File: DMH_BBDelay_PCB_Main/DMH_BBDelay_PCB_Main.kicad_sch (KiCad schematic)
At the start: 0 parts

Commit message: Started designing schematic
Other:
- added sheet Attenuverters (Attenuverters.kicad_sch)
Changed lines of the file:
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@@
 		)
 		(instances
-			(project "DMH-Kosmo-10cm-PCB"
+			(project "DMH_BBDelay_PCB_Main"
 				(path "/58f4306d-5387-4983-bb08-41a2313fd315"
 					(page "4")
@@
 		)
 		(instances
-			(project "DMH-Kosmo-10cm-PCB"
+			(project "DMH_BBDelay_PCB_Main"
 				(path "/58f4306d-5387-4983-bb08-41a2313fd315"
 					(page "3")
@@
 		)
 		(instances
-			(project "DMH-Kosmo-10cm-PCB"
+			(project "DMH_BBDelay_PCB_Main"
 				(path "/58f4306d-5387-4983-bb08-41a2313fd315"
 					(page "2")
 				)
 			)
+		)
+	)
+	(sheet
+		(at 63.5 152.4)
+		(size 25.4 25.4)
+		(exclude_from_sim no)
+		(in_bom yes)
+		(on_board yes)
+		(dnp no)
+		(fields_autoplaced yes)
+		(stroke
+			(width 0.1524)
+			(type solid)
+		)
+		(fill
+			(color 0 0 0 0)
+		)
+		(property "Sheetname" "Attenuverters"
+			(at 63.5 151.6884 0)
+			(show_name no)
+			(do_not_autoplace no)
+			(effects
+				(font
+					(size 1.27 1.27)
+					(thickness 0.254)
+					(bold yes)
+					(italic yes)
+				)
+				(justify left bottom)
+			)
+		)
+		(property "Sheetfile" "Attenuverters.kicad_sch"
+			(at 63.5 178.3846 0)
+			(hide yes)
+			(show_name no)
+			(do_not_autoplace no)
+			(effects
+				(font
+					(size 1.27 1.27)
+				)
+				(justify left top)
+			)
+		)
+		(instances
+			(project "DMH_BBDelay_PCB_Main"
+				(path "/58f4306d-5387-4983-bb08-41a2313fd315"
+					(page "6")
+				)
+			)

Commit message: Schematic in progress
Next is implementation of Channel B, CV Linking and Ping-Pong mode
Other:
- title: (none) -> 3205 Delay
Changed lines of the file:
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@@
 	(paper "A4")
 	(title_block
+		(title "3205 Delay")
 		(rev "1")
 		(company "DMH Instruments")

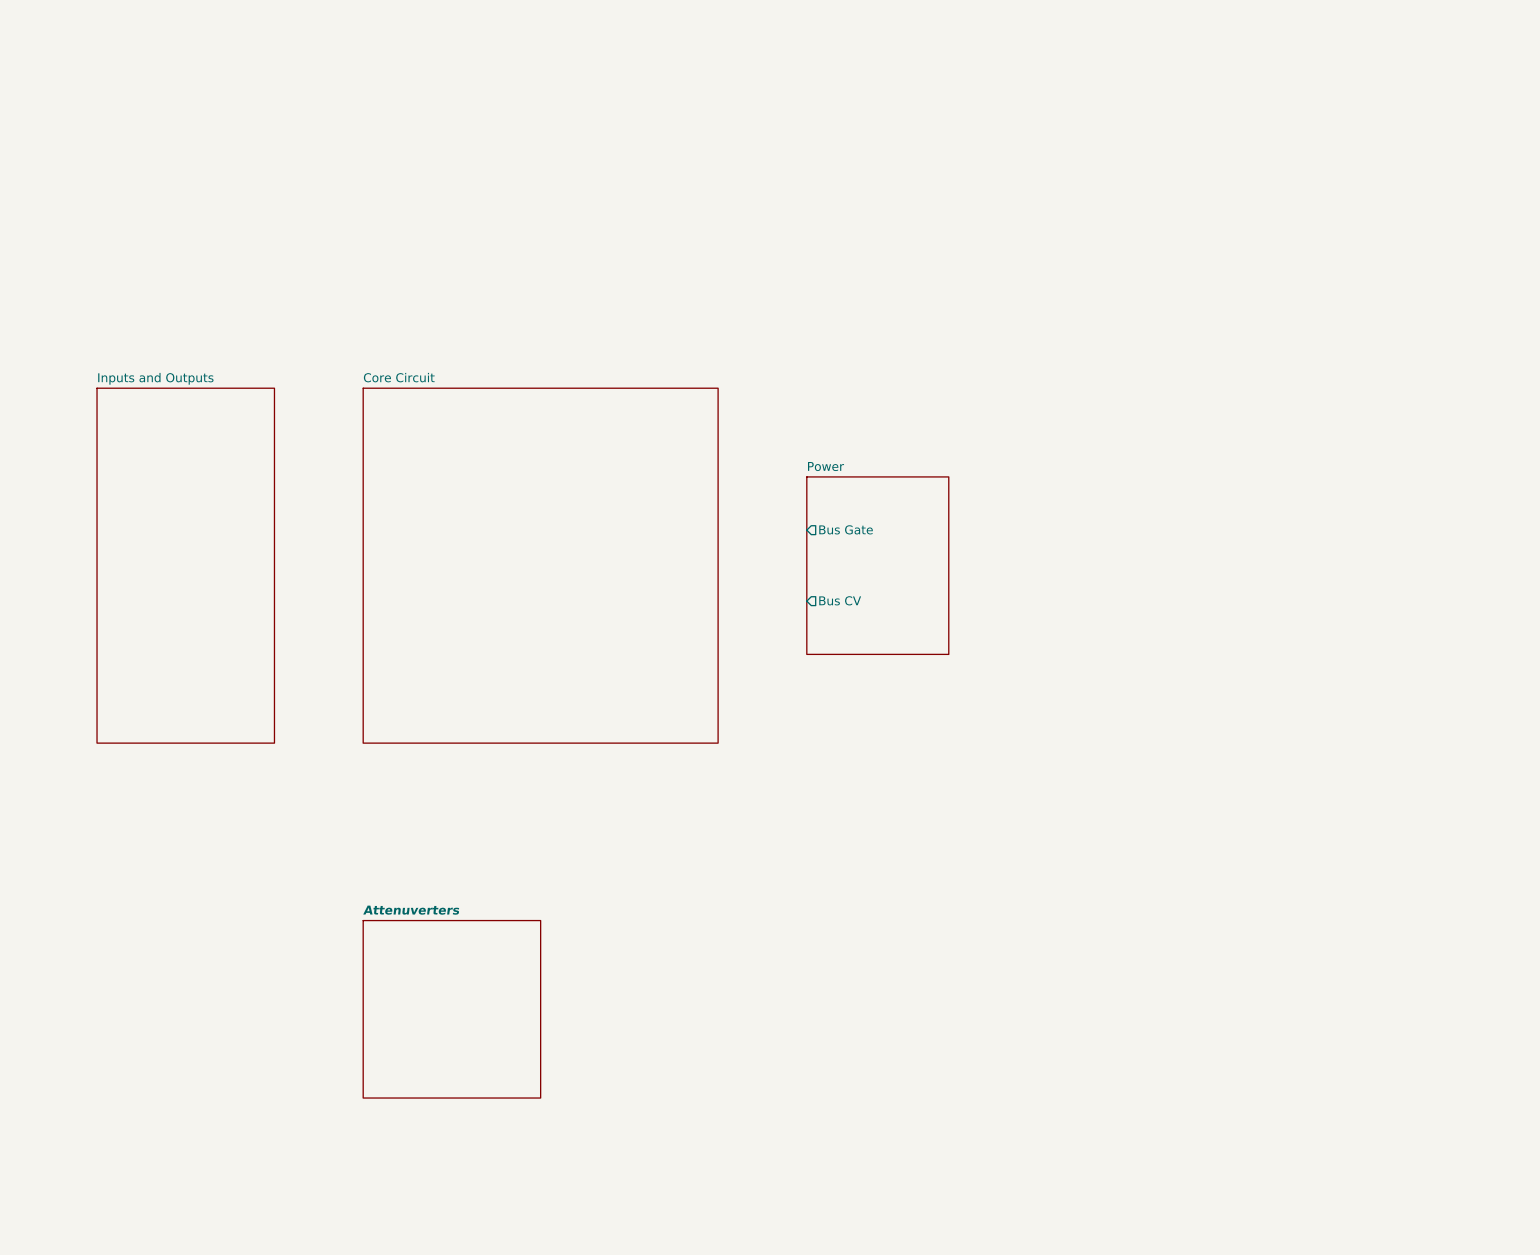
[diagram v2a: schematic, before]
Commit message: Implemented Link switch in schematic
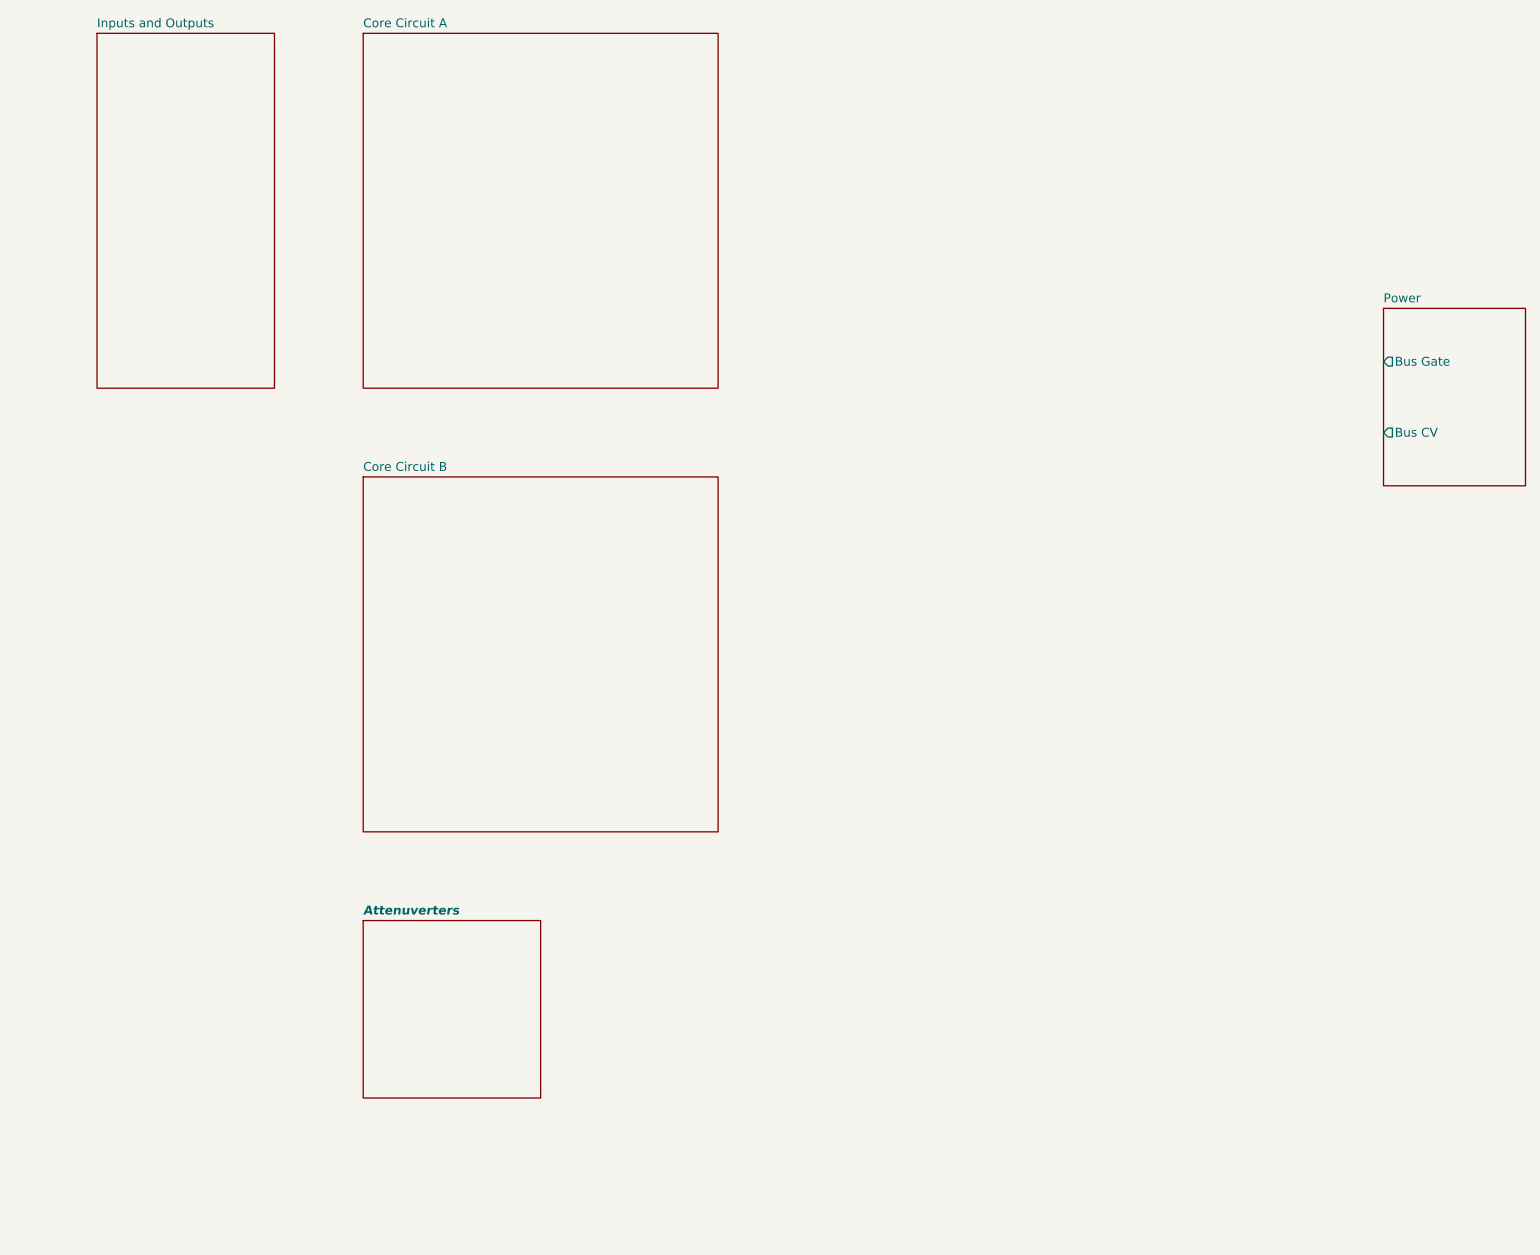
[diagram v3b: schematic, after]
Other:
- sheet Core Circuit renamed Core Circuit A
- added sheet Core Circuit B (Core_Circuit_B.kicad_sch)
- sheet Core Circuit A: file Core_Circuit.kicad_sch -> Core_Circuit_A.kicad_sch
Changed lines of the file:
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@@
 	)
 	(sheet
-		(at 127 88.9)
+		(at 209.55 64.77)
 		(size 20.32 25.4)
 		(exclude_from_sim no)
@@
 		)
 		(property "Sheetname" "Power"
-			(at 127 88.1884 0)
+			(at 209.55 64.0584 0)
 			(show_name no)
 			(do_not_autoplace no)
@@
 		)
 		(property "Sheetfile" "Power.kicad_sch"
-			(at 127 114.8846 0)
+			(at 209.55 90.7546 0)
 			(hide yes)
 			(show_name no)
@@
 		)
 		(pin "Bus Gate" output
-			(at 127 96.52 180)
+			(at 209.55 72.39 180)
 			(effects
 				(font
@@
 		)
 		(pin "Bus CV" output
-			(at 127 106.68 180)
+			(at 209.55 82.55 180)
 			(effects
 				(font
@@
 	)
 	(sheet
-		(at 63.5 76.2)
+		(at 63.5 88.9)
 		(size 50.8 50.8)
 		(exclude_from_sim no)
@@
 			(color 0 0 0 0)
 		)
-		(property "Sheetname" "Core Circuit"
-			(at 63.5 75.4884 0)
+		(property "Sheetname" "Core Circuit B"
+			(at 63.5 88.1884 0)
 			(show_name no)
 			(do_not_autoplace no)
@@
 			)
 		)
-		(property "Sheetfile" "Core_Circuit.kicad_sch"
-			(at 63.5 127.5846 0)
+		(property "Sheetfile" "Core_Circuit_B.kicad_sch"
+			(at 63.5 140.2846 0)
+			(hide yes)
+			(show_name no)
+			(do_not_autoplace no)
+			(effects
+				(font
+					(size 1.27 1.27)
+				)
+				(justify left top)
+			)
+		)
+		(instances
+			(project "DMH_BBDelay_PCB_Main"
+				(path "/58f4306d-5387-4983-bb08-41a2313fd315"
+					(page "8")
+				)
+			)
+		)
+	)
+	(sheet
+		(at 63.5 25.4)
+		(size 50.8 50.8)
+		(exclude_from_sim no)
+		(in_bom yes)
+		(on_board yes)
+		(dnp no)
+		(fields_autoplaced yes)
+		(stroke
+			(width 0.1524)
+			(type solid)
+		)
+		(fill
+			(color 0 0 0 0)
+		)
+		(property "Sheetname" "Core Circuit A"
+			(at 63.5 24.6884 0)
+			(show_name no)
+			(do_not_autoplace no)
+			(effects
+				(font
+					(size 1.27 1.27)
+				)
+				(justify left bottom)
+			)
+		)
+		(property "Sheetfile" "Core_Circuit_A.kicad_sch"
+			(at 63.5 76.7846 0)
 			(hide yes)
 			(show_name no)
@@
 	)
 	(sheet
-		(at 25.4 76.2)
+		(at 25.4 25.4)
 		(size 25.4 50.8)
 		(exclude_from_sim no)
@@
 		)
 		(property "Sheetname" "Inputs and Outputs"
-			(at 25.4 75.4884 0)
+			(at 25.4 24.6884 0)
 			(show_name no)
 			(do_not_autoplace no)
@@
 		)
 		(property "Sheetfile" "Inputs_and_Outputs.kicad_sch"
-			(at 25.4 127.5846 0)
+			(at 25.4 76.7846 0)
 			(hide yes)
 			(show_name no)

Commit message: Implemented tone control
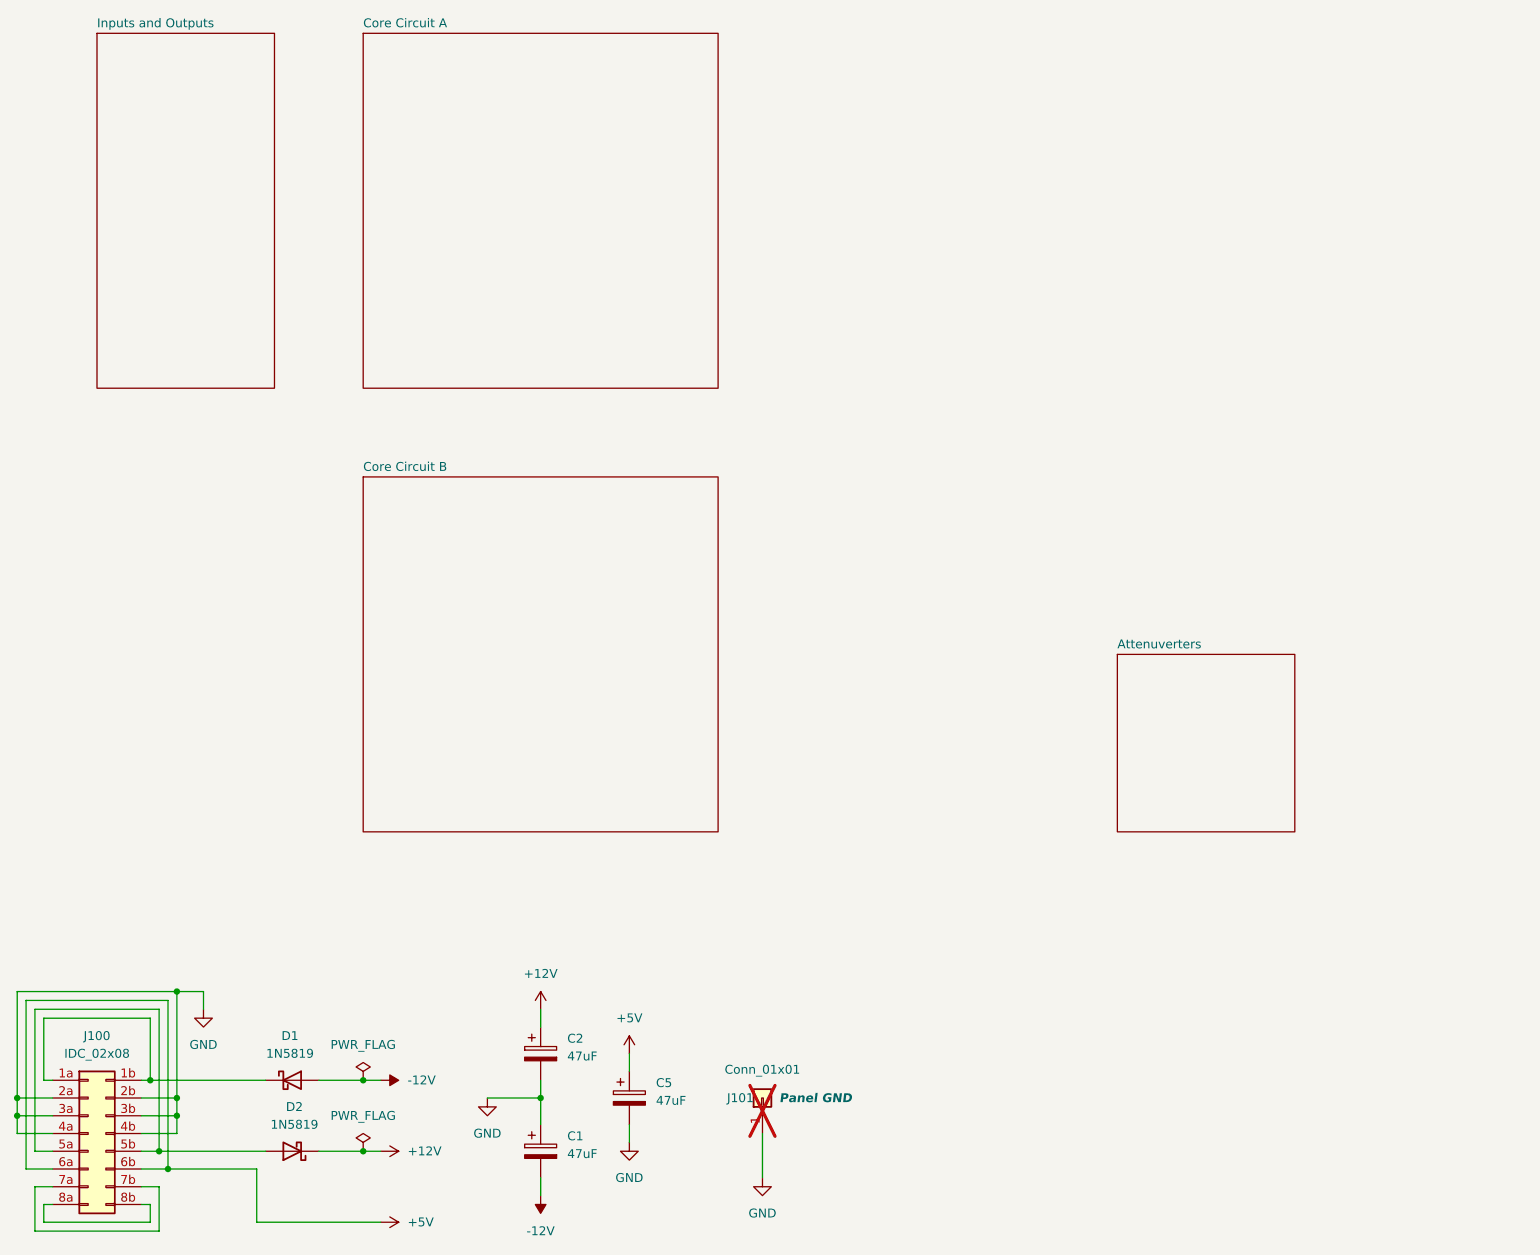
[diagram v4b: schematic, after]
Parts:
- added C1, C2: 47uF, Capacitor_THT:CP_Radial_D5.0mm_P2.00mm, symbol Device:C_Polarized
- added C5: 47uF, Capacitor_THT:CP_Radial_D4.0mm_P1.50mm, symbol Device:C_Polarized
- added D1, D2: 1N5819, Diode_THT:D_DO-41_SOD81_P10.16mm_Horizontal, symbol Diode:1N5819
- added J100: IDC_02x08, SynthStuff:IDC-Header_2x08_P2.54mm_Vertical_Eurorack, symbol SynthStuff:Eurorack_Power_Connector_16Pin
- added J101: Conn_01x01, Connector_PinHeader_2.54mm:PinHeader_1x01_P2.54mm_Vertical, symbol Connector_Generic:Conn_01x01
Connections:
- new net: D1.1 (K), J100.1a (Pin_1a), J100.1b (Pin_1b)
- new net: D2.2 (A), J100.5a (Pin_5a), J100.5b (Pin_5b)
- new net: J100.7a (Pin_7a), J100.7b (Pin_7b)
- new net: J100.8a (Pin_8a), J100.8b (Pin_8b)
- new net +12V: C2.1, D2.1 (K)
- new net +5V: C5.1, J100.6a (Pin_6a), J100.6b (Pin_6b)
- new net -12V: C1.2, D1.2 (A)
- new net GND: C1.1, C2.2, C5.2, J100.2a (Pin_2a), J100.2b (Pin_2b), J100.3a (Pin_3a), J100.3b (Pin_3b), J100.4a (Pin_4a), J100.4b (Pin_4b), J101.1 (Pin_1)
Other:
- removed sheet Power

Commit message: Schematic ready for breadboarding
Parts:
- renumbered J101 to J9
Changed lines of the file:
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@@
 		(in_pos_files yes)
 		(dnp yes)
-		(property "Reference" "J101"
+		(property "Reference" "J9"
 			(at 115.57 177.8 90)
 			(show_name no)
@@
 			(project "DMH_BBDelay_PCB_Main"
 				(path "/58f4306d-5387-4983-bb08-41a2313fd315"
-					(reference "J101")
+					(reference "J9")
 					(unit 1)
 				)
@@
 	)
 	(sheet
-		(at 171.45 114.3)
+		(at 25.4 101.6)
 		(size 25.4 25.4)
 		(exclude_from_sim no)
@@
 		)
 		(property "Sheetname" "Attenuverters"
-			(at 171.45 113.5884 0)
+			(at 25.4 100.8884 0)
 			(show_name no)
 			(do_not_autoplace no)
@@
 		)
 		(property "Sheetfile" "Attenuverters.kicad_sch"
-			(at 171.45 140.2846 0)
-			(hide yes)
-			(show_name no)
+			(at 25.4 127.5846 0)
+			(hide yes)
+			(show_name no)

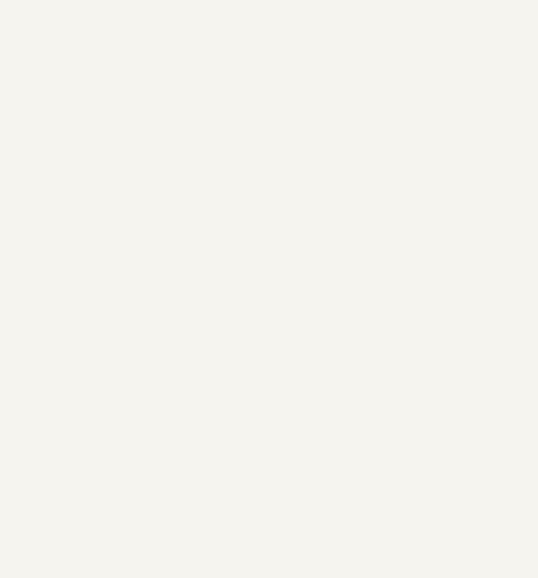
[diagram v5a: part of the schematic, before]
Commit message: Moved LEDs to own page
... so I can add the LED control via CD4040
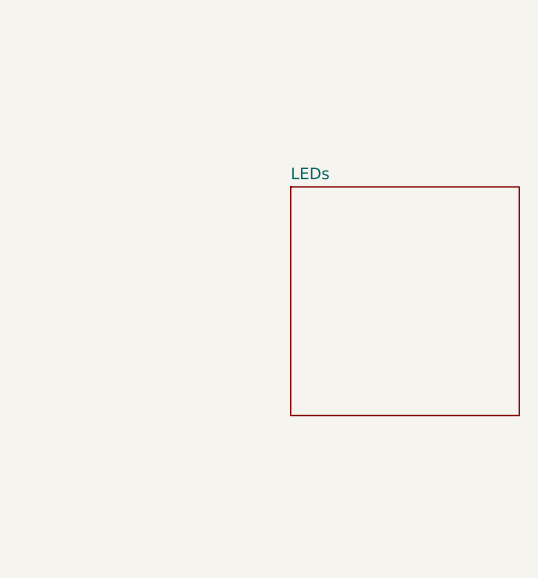
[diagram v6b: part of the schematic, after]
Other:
- added sheet LEDs (LEDs.kicad_sch)
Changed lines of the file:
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@@
+	)
+	(sheet
+		(at 165.1 63.5)
+		(size 25.4 25.4)
+		(exclude_from_sim no)
+		(in_bom yes)
+		(on_board yes)
+		(dnp no)
+		(fields_autoplaced yes)
+		(stroke
+			(width 0.1524)
+			(type solid)
+		)
+		(fill
+			(color 0 0 0 0)
+		)
+		(property "Sheetname" "LEDs"
+			(at 165.1 62.7884 0)
+			(show_name no)
+			(do_not_autoplace no)
+			(effects
+				(font
+					(size 1.27 1.27)
+				)
+				(justify left bottom)
+			)
+		)
+		(property "Sheetfile" "LEDs.kicad_sch"
+			(at 165.1 89.4846 0)
+			(hide yes)
+			(show_name no)
+			(do_not_autoplace no)
+			(effects
+				(font
+					(size 1.27 1.27)
+				)
+				(justify left top)
+			)
+		)
+		(instances
+			(project "DMH_BBDelay_PCB_Main"
+				(path "/58f4306d-5387-4983-bb08-41a2313fd315"
+					(page "12")
+				)
+			)
+		)
 	)
 	(sheet
